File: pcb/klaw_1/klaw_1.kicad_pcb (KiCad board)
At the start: 2 copper layers, 128.6 x 98.5 mm, 71 parts, among them J1 PJ-320A-4P, J3 lv27, SW1 SW_PUSH-MX_W_LED, SW10 SW_PUSH-MX_W_LED, SW12 SW_PUSH-MX_W_LED, SW13 SW_PUSH-MX_W_LED, SW14 SW_PUSH-MX_W_LED, SW15 SW_PUSH-MX_W_LED, SW16 SW_PUSH-MX_W_LED, SW18 EC11E15244G1, SW2 SW_PUSH-MX_W_LED, SW20 SW_PUSH-MX_W_LED, SW21 SW_PUSH-MX_W_LED, SW3 SW_PUSH-MX_W_LED, SW4 SW_PUSH-MX_W_LED, SW5 SW_PUSH-MX_W_LED, SW6 SW_PUSH-MX_W_LED, SW7 SW_PUSH-MX_W_LED, SW8 SW_PUSH-MX_W_LED, SW9 SW_PUSH-MX_W_LED, U1 ProMicro

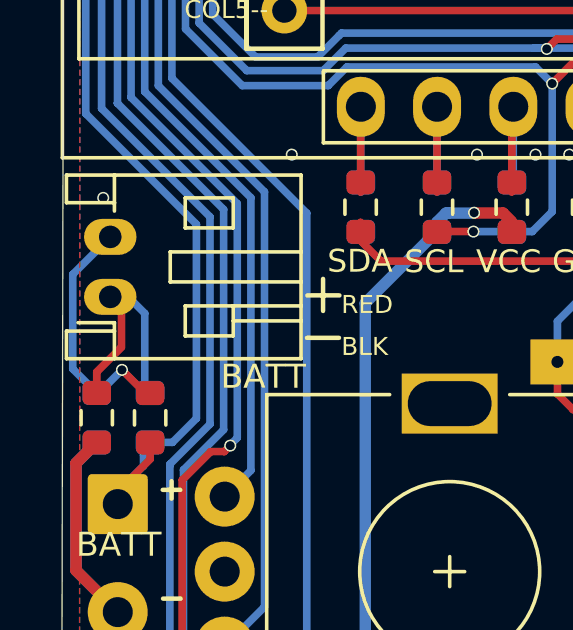
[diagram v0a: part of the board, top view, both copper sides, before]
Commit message: feat: 3D view depicts one consistent build (right-hand)
- left-build option-resistor models hidden per instance (display
  only; CPLs/BOMs unaffected - both builds still orderable)
- LED models flipped to the component face, completing the
  right-build depiction; remaining flips synced into the board
- doc renders refreshed
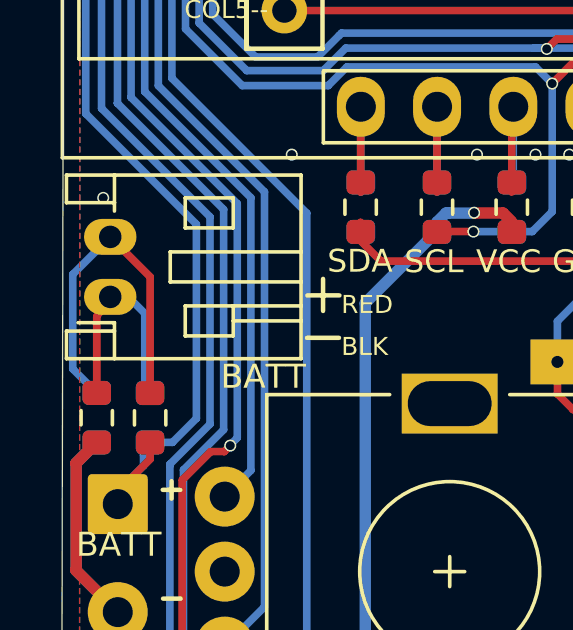
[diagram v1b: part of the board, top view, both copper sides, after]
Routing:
- net /PAD2: track 8.22 -> 11.8 mm, vias 1 -> 0
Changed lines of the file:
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@@
 		(embedded_fonts no)
 		(model "${KIPRJMOD}/klaw.3dshapes/R_0603_1608Metric.step"
+			(hide yes)
 			(offset
 				(xyz 0 0 0)
@@
 		(model "${KIPRJMOD}/klaw.3dshapes/LED_SK6812MINI-EA.step"
 			(offset
-				(xyz 0 -5.5 0)
+				(xyz 0 -5.5 -1.6)
 			)
 			(scale
@@
 			)
 			(rotate
-				(xyz 0 0 180)
+				(xyz 180 0 0)
 			)
 		)
@@
 		(model "${KIPRJMOD}/klaw.3dshapes/LED_SK6812MINI-EA.step"
 			(offset
-				(xyz 0 -5.5 0)
+				(xyz 0 -5.5 -1.6)
 			)
 			(scale
@@
 			)
 			(rotate
-				(xyz 0 0 180)
+				(xyz 180 0 0)
 			)
 		)
@@
 		(model "${KIPRJMOD}/klaw.3dshapes/LED_SK6812MINI-EA.step"
 			(offset
-				(xyz 0 -5.5 0)
+				(xyz 0 -5.5 -1.6)
 			)
 			(scale
@@
 			)
 			(rotate
-				(xyz 0 0 180)
+				(xyz 180 0 0)
 			)
 		)
@@
 		(model "${KIPRJMOD}/klaw.3dshapes/LED_SK6812MINI-EA.step"
 			(offset
-				(xyz 0 -5.5 0)
+				(xyz 0 -5.5 -1.6)
 			)
 			(scale
@@
 			)
 			(rotate
-				(xyz 0 0 180)
+				(xyz 180 0 0)
 			)
 		)
@@
 		(model "${KIPRJMOD}/klaw.3dshapes/LED_SK6812MINI-EA.step"
 			(offset
-				(xyz 0 -5.5 0)
+				(xyz 0 -5.5 -1.6)
 			)
 			(scale
@@
 			)
 			(rotate
-				(xyz 0 0 180)
+				(xyz 180 0 0)
 			)
 		)
@@
 		(model "${KIPRJMOD}/klaw.3dshapes/LED_SK6812MINI-EA.step"
 			(offset
-				(xyz 0 -5.5 0)
+				(xyz 0 -5.5 -1.6)
 			)
 			(scale
@@
 			)
 			(rotate
-				(xyz 0 0 180)
+				(xyz 180 0 0)
 			)
 		)
@@
 		(model "${KIPRJMOD}/klaw.3dshapes/LED_SK6812MINI-EA.step"
 			(offset
-				(xyz 0 -5.5 0)
+				(xyz 0 -5.5 -1.6)
 			)
 			(scale
@@
 			)
 			(rotate
-				(xyz 0 0 180)
+				(xyz 180 0 0)
 			)
 		)
@@
 		(model "${KIPRJMOD}/klaw.3dshapes/JST_PH_S2B-PH-K.step"
 			(offset
-				(xyz 0 0 0)
+				(xyz 0 0 -1.6)
 			)
 			(scale
@@
 			)
 			(rotate
-				(xyz 0 0 0)
+				(xyz 0 180 0)
 			)
 		)
@@
 		(model "${KIPRJMOD}/klaw.3dshapes/LED_SK6812MINI-EA.step"
 			(offset
-				(xyz 0 -5.5 0)
+				(xyz 0 -5.5 -1.6)
 			)
 			(scale
@@
 			)
 			(rotate
-				(xyz 0 0 180)
+				(xyz 180 0 0)
 			)
 		)
@@
 		(model "${KIPRJMOD}/klaw.3dshapes/SKRTLAE010.step"
 			(offset
-				(xyz 0 0 0)
+				(xyz 0 0 -1.6)
 			)
 			(scale
@@
 			)
 			(rotate
-				(xyz 0 0 0)
+				(xyz 0 180 0)
 			)
 		)
@@
 		(model "${KIPRJMOD}/klaw.3dshapes/LED_SK6812MINI-EA.step"
 			(offset
-				(xyz 0 -5.5 0)
+				(xyz 0 -5.5 -1.6)
 			)
 			(scale
@@
 			)
 			(rotate
-				(xyz 0 0 180)
+				(xyz 180 0 0)
 			)
 		)
@@
 		(model "${KIPRJMOD}/klaw.3dshapes/LED_SK6812MINI-EA.step"
 			(offset
-				(xyz 0 -5.5 0)
+				(xyz 0 -5.5 -1.6)
 			)
 			(scale
@@
 			)
 			(rotate
-				(xyz 0 0 180)
+				(xyz 180 0 0)
 			)
 		)
@@
 		(model "${KIPRJMOD}/klaw.3dshapes/LED_SK6812MINI-EA.step"
 			(offset
-				(xyz 0 -5.5 0)
+				(xyz 0 -5.5 -1.6)
 			)
 			(scale
@@
 			)
 			(rotate
-				(xyz 0 0 180)
+				(xyz 180 0 0)
 			)
 		)
@@
 		(model "${KIPRJMOD}/klaw.3dshapes/LED_SK6812MINI-EA.step"
 			(offset
-				(xyz 0 -5.5 0)
+				(xyz 0 -5.5 -1.6)
 			)
 			(scale
@@
 			)
 			(rotate
-				(xyz 0 0 180)
+				(xyz 180 0 0)
 			)
 		)
@@
 		(model "${KIPRJMOD}/klaw.3dshapes/LED_SK6812MINI-EA.step"
 			(offset
-				(xyz 0 -5.5 0)
+				(xyz 0 -5.5 -1.6)
 			)
 			(scale
@@
 			)
 			(rotate
-				(xyz 0 0 180)
+				(xyz 180 0 0)
 			)
 		)
@@
 		(model "${KIPRJMOD}/klaw.3dshapes/LED_SK6812MINI-EA.step"
 			(offset
-				(xyz 0 -5.5 0)
+				(xyz 0 -5.5 -1.6)
 			)
 			(scale
@@
 			)
 			(rotate
-				(xyz 0 0 180)
+				(xyz 180 0 0)
 			)
 		)
@@
 		(model "${KIPRJMOD}/klaw.3dshapes/MSK12C02.step"
 			(offset
-				(xyz 1.35 -3.75 0)
+				(xyz -1.35 -3.75 -1.6)
 			)
 			(scale
@@
 			)
 			(rotate
-				(xyz -0 -0 -90)
+				(xyz 0 180 90)
 			)
 		)
@@
 		(embedded_fonts no)
 		(model "${KIPRJMOD}/klaw.3dshapes/R_0603_1608Metric.step"
+			(hide yes)
 			(offset
 				(xyz 0 0 0)
@@
 		(model "${KIPRJMOD}/klaw.3dshapes/LED_SK6812MINI-EA.step"
 			(offset
-				(xyz 0 -5.5 0)
+				(xyz 0 -5.5 -1.6)
 			)
 			(scale
@@
 			)
 			(rotate
-				(xyz 0 0 180)
+				(xyz 180 0 0)
 			)
 		)
@@
 		(model "${KIPRJMOD}/klaw.3dshapes/LED_SK6812MINI-EA.step"
 			(offset
-				(xyz 0 -5.5 0)
+				(xyz 0 -5.5 -1.6)
 			)
 			(scale
@@
 			)
 			(rotate
-				(xyz 0 0 180)
+				(xyz 180 0 0)
 			)
 		)
@@
 		(model "${KIPRJMOD}/klaw.3dshapes/LED_SK6812MINI-EA.step"
 			(offset
-				(xyz 0 -5.5 0)
+				(xyz 0 -5.5 -1.6)
 			)
 			(scale
@@
 			)
 			(rotate
-				(xyz 0 0 180)
+				(xyz 180 0 0)
 			)
 		)
@@
 		(embedded_fonts no)
 		(model "${KIPRJMOD}/klaw.3dshapes/R_0603_1608Metric.step"
+			(hide yes)
 			(offset
 				(xyz 0 0 0)
@@
 		(embedded_fonts no)
 		(model "${KIPRJMOD}/klaw.3dshapes/R_0603_1608Metric.step"
+			(hide yes)
 			(offset
 				(xyz 0 0 0)
@@
 		(embedded_fonts no)
 		(model "${KIPRJMOD}/klaw.3dshapes/R_0603_1608Metric.step"
+			(hide yes)
 			(offset
 				(xyz 0 0 0)
@@
 		(embedded_fonts no)
 		(model "${KIPRJMOD}/klaw.3dshapes/R_0603_1608Metric.step"
+			(hide yes)
 			(offset
 				(xyz 0 0 0)
@@
 		(embedded_fonts no)
 		(model "${KIPRJMOD}/klaw.3dshapes/R_0603_1608Metric.step"
+			(hide yes)
 			(offset
 				(xyz 0 0 0)
@@
 		(embedded_fonts no)
 		(model "${KIPRJMOD}/klaw.3dshapes/R_0603_1608Metric.step"
+			(hide yes)
 			(offset
 				(xyz 0 0 0)
@@
 		(embedded_fonts no)
 		(model "${KIPRJMOD}/klaw.3dshapes/R_0603_1608Metric.step"
+			(hide yes)
 			(offset
 				(xyz 0 0 0)
@@
 	)
 	(segment
-		(start 83.825 107.29266)
-		(end 84.65 106.46766)
-		(width 0.254)
-		(layer "F.Cu")
-		(net "/PAD1")
-	)
-	(segment
-		(start 84.65 106.46766)
-		(end 84.65 105.16766)
+		(start 83.825 107.9919)
+		(end 83.825 105.45)
 		(width 0.254)
 		(layer "F.Cu")
@@
 	)
 	(segment
-		(start 83.825 107.9919)
-		(end 83.825 107.29266)
+		(start 83.825 105.45)
+		(end 84.275 104.79266)
 		(width 0.254)
 		(layer "F.Cu")
@@
 	)
 	(segment
-		(start 85.430877 107.9919)
-		(end 84.66476 107.225783)
+		(start 84.275 102.79266)
+		(end 85.605046 104.122706)
 		(width 0.254)
 		(layer "F.Cu")
 		(net "/PAD2")
 	)
-	(via
-		(at 84.66476 107.225783)
-		(size 0.4)
-		(drill 0.3)
-		(layers "F.Cu" "B.Cu")
-		(capping no)
-		(covering
-			(front no)
-			(back no)
-		)
-		(plugging
-			(front no)
-			(back no)
-		)
-		(filling no)
+	(segment
+		(start 85.605046 104.122706)
+		(end 85.605046 108)
+		(width 0.254)
+		(layer "F.Cu")
 		(net "/PAD2")
 	)
@@
 	)
 	(segment
-		(start 83.898263 107.99228)
-		(end 84.66476 107.225783)
-		(width 0.254)
-		(layer "B.Cu")
-		(net "/PAD2")
-	)
-	(segment
 		(start 83.025 104.04266)
 		(end 84.275 102.79266)
@@
 		)
 		(min_thickness 0.254)
-		(fill
+		(fill yes
 			(mode hatch)
 			(thermal_gap 0.508)
